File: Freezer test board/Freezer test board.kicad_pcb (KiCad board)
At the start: 4 copper layers, 89.9 x 104.9 mm, 18 parts, among them J1 TB007-508-03BE, J2 TB007-508-03BE, J3 TB007-508-03BE, J4 TB007-508-03BE, J5 TB007-508-03BE, J6 TB007-508-03BE, J7 Conn_02x20_Odd_Even, J8 Conn_02x02_Odd_Even

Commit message: temp commit
I just curved the edges of the PCB and un-did all the connection
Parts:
- H1, H2, H3, H4, J1, J2, J3, J4, J5, J6, J7, R1, R2, R3, R4, R5, R6: moved to F.Cu
- J8: moved to B.Cu
- moved H1 78.2 mm to (90.1, 40.7), turned to 0 degrees
- moved H2 78.2 mm to (90.1, 98.7), turned to 0 degrees
- moved J7 75.7 mm to (91.4, 45.6), turned to 0 degrees
- moved J1 73.4 mm to (165.9, 41.0)
- moved J2 73.4 mm to (165.9, 58.1)
- moved J3 73.4 mm to (165.9, 74.7)
- moved J4 73.4 mm to (165.9, 91.9)
- moved J5 73.4 mm to (165.9, 108.6)
- moved J6 73.4 mm to (165.9, 125.6)
- moved R1 38.1 mm to (148.3, 46.1), turned to 0 degrees
- moved R2 38.1 mm to (148.3, 63.2), turned to 0 degrees
- moved R3 38.1 mm to (148.3, 79.8), turned to 0 degrees
- moved R4 38.1 mm to (148.3, 97.0), turned to 0 degrees
- moved R5 38.1 mm to (148.3, 113.7), turned to 0 degrees
- moved R6 38.1 mm to (148.3, 130.7), turned to 0 degrees
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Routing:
- net 3V3: track 549.0 -> 0.33 mm
- net GND: track 510.4 -> 0.25 mm
- net GPIO26: track 72.8 -> 0.00 mm, vias 1 -> 0
- net GPIO6: track 69.0 -> 0.00 mm, vias 1 -> 0
- net GPIO22: track 63.3 -> 0.00 mm, vias 1 -> 0
- net GPIO5: track 63.1 -> 0.00 mm, vias 1 -> 0
- net GPIO17: track 61.6 -> 0.00 mm, vias 1 -> 0
- net GPIO27: track 57.5 -> 0.00 mm, vias 1 -> 0
- net Net-(J2-Signal): track 17.4 -> 0.00 mm, vias 1 -> 0
- net Net-(J1-Signal): track 17.3 -> 0.00 mm, vias 1 -> 0
- net Net-(J3-Signal): track 17.3 -> 0.00 mm, vias 1 -> 0
- net Net-(J4-Signal): track 17.3 -> 0.00 mm, vias 1 -> 0
- net Net-(J6-Signal): track 17.3 -> 0.00 mm, vias 1 -> 0
- net Net-(J5-Signal): track 17.3 -> 0.00 mm, vias 1 -> 0
- added copper zone on In2.Cu, net 3V3
- added copper zone on B.Cu, net GPIO17
- added copper zone on F.Cu, net GPIO17
- added copper zone on In1.Cu, net GPIO17
- removed copper zone on B.Cu, net GND
- removed copper zone on F.Cu, net GND
- removed copper zone on In1.Cu, net GND
- removed copper zone on In2.Cu, net GND
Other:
- outline, holes or cut-outs redrawn

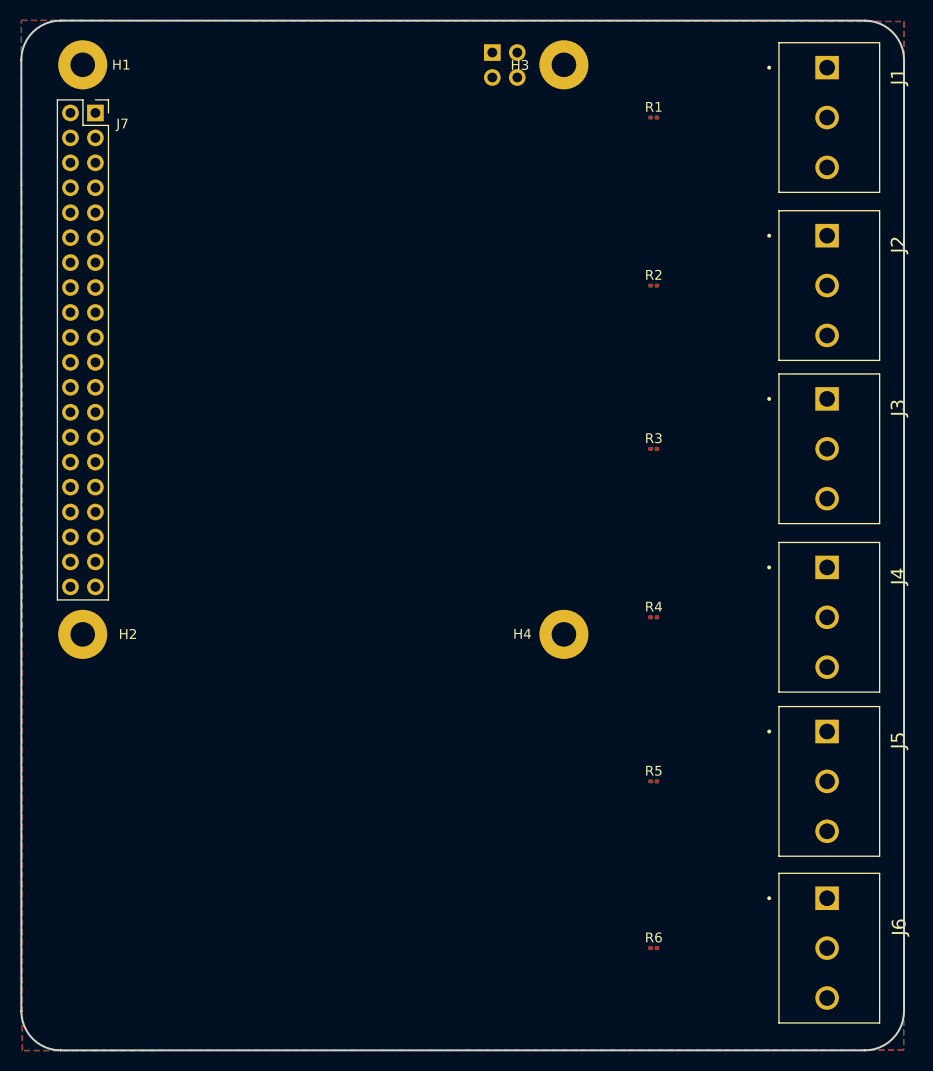
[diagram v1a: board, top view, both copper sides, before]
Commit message: Temporary Push
At the moment the most recent changes Made are the following: board has been shrunk by moving the terminal blocks in-between the mounting holes, the terminal blocks have been changed from 5.08mm to 3.54mm. The layers have been changed from SIG-GND-PWR-GND to SIG-GND-PWR-SIG2. Then all of the connections have been removed. No schematic changes
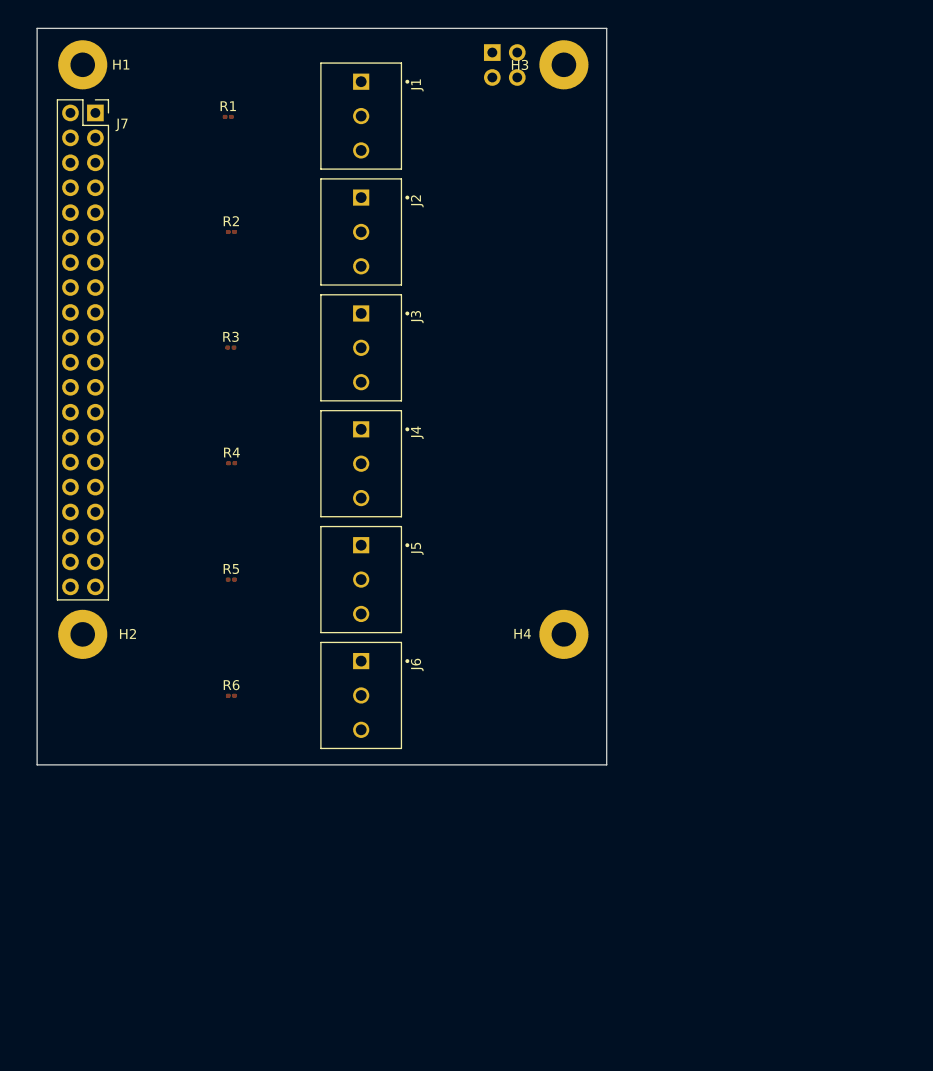
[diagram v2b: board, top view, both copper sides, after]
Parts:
- J1, J2, J3, J4, J5, J6: value TB007-508-03BE -> 284391-3; footprint TB007-508-03BE:CUI_TB007-508-03BE -> 284391_3:TE_284391-3
- moved J6 51.7 mm to (118.5, 104.9)
- moved R6 50.1 mm to (105.3, 105.0)
- moved J5 49.9 mm to (118.5, 93.1)
- moved J4 48.6 mm to (118.5, 81.3)
- moved J3 47.7 mm to (118.5, 69.5)
- moved J1 47.7 mm to (118.5, 45.9)
- moved R5 47.7 mm to (105.3, 93.1)
- moved J2 47.4 mm to (118.5, 57.7)
- moved R4 45.8 mm to (105.3, 81.3)
- moved R3 44.3 mm to (105.2, 69.5)
- moved R2 43.4 mm to (105.3, 57.7)
- moved R1 43.3 mm to (105.0, 46.0)
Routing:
- removed copper zone on In2.Cu, net 3V3
- removed copper zone on B.Cu, net GPIO17
- removed copper zone on F.Cu, net GPIO17
- removed copper zone on In1.Cu, net GPIO17
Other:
- board size 89.9 x 104.9 mm -> 58 x 75 mm

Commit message: Uh
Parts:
- moved R6 0.38 mm to (104.9, 104.8)
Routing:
- net 3V3: track 0.00 -> 204.9 mm
- net GND: track 0.00 -> 184.5 mm
- net GPIO26: track 0.00 -> 19.0 mm
- net GPIO17: track 0.00 -> 18.3 mm
- net GPIO6: track 0.00 -> 17.4 mm
- net GPIO22: track 0.00 -> 16.0 mm
- net GPIO27: track 0.00 -> 14.8 mm
- net GPIO5: track 0.00 -> 13.6 mm
- net Net-(J6-DATA): track 0.00 -> 13.3 mm
- net Net-(J1-DATA): track 0.00 -> 13.3 mm
- net Net-(J3-DATA): track 0.00 -> 13.0 mm
- net Net-(J5-DATA): track 0.00 -> 12.9 mm
- net Net-(J2-DATA): track 0.00 -> 12.9 mm
- net Net-(J4-DATA): track 0.00 -> 12.9 mm
- added copper zone on In2.Cu, net 3V3
- added copper zone on In1.Cu, net GND
- added copper zone on F.Cu, net GPIO26
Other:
- outline, holes or cut-outs redrawn

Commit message: changes layouts
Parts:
- removed J1: 284391-3, 284391_3:TE_284391-3
- removed the J2 at (118.5, 57.7)
- removed the R1 at (105.0, 46.0)
- added J7: 284391-3, 284391_3:TE_284391-3, F.Cu at (136.0, 73.5)
- added J9: 284391-3, 284391_3:TE_284391-3, F.Cu at (136.0, 49.5)
- added R3: 4.7k, Resistor_SMD:R_0201_0603Metric, F.Cu at (120.8, 48.8)
- added R7: 4.7k, Resistor_SMD:R_0201_0603Metric, F.Cu at (120.7, 87.7)
- J8: value Conn_02x02_Odd_Even -> 284391-3; footprint Connector_PinSocket_2.54mm:PinSocket_2x02_P2.54mm_Vertical -> 284391_3:TE_284391-3; moved to F.Cu
- moved R6 53.3 mm to (120.8, 54.0)
- moved J2 48.2 mm to (89.0, 93.7), turned to 180 degrees
- moved R5 43.7 mm to (120.8, 52.2)
- moved R4 34.5 mm to (120.8, 50.5)
- moved J3 32.1 mm to (101.0, 96.5), turned to 180 degrees
- moved J6 26.1 mm to (136.0, 85.5)
- moved R2 25.6 mm to (128.5, 47.0)
- moved J8 22.4 mm to (136.0, 61.5), turned to -90 degrees
- moved R1 18.9 mm to (120.5, 58.3)
- moved J4 16.1 mm to (113.0, 96.5), turned to 180 degrees
- moved J5 7.32 mm to (125.0, 96.5), turned to 180 degrees
- moved H4 1.16 mm to (138.0, 98.5)
- moved H1 1.16 mm to (89.0, 40.5)
- moved H2 1.16 mm to (89.0, 98.5)
- moved H3 1.15 mm to (138.0, 40.7)
- renumbered J7 to J2, R3 to R1
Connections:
- J2 pad 1: 3V3 -> +3V3
- J3 pad 1: 3V3 -> +3V3
- J3 pad 2: Net-(J3-DATA) -> GPIO17
- J4 pad 1: 3V3 -> +3V3
- J4 pad 2: Net-(J4-DATA) -> GPIO27
- J5 pad 1: 3V3 -> +3V3
- J5 pad 2: Net-(J5-DATA) -> GPIO22
- J6 pad 1: 3V3 -> +3V3
- J6 pad 2: Net-(J6-DATA) -> GPIO5
- J8 pad 1: unconnected-(J8-Pin_1-Pad1) -> +3V3
- J8 pad 2: unconnected-(J8-Pin_2-Pad2) -> GPIO26
- J8 pad 3: unconnected-(J8-Pin_3-Pad3) -> GND
- R1 pad 1: GPIO22 -> GPIO17
- R1 pad 2: Net-(J3-DATA) -> +3V3
- R2 pad 2: Net-(J2-DATA) -> +3V3
- R4 pad 2: Net-(J4-DATA) -> +3V3
- R5 pad 2: Net-(J5-DATA) -> +3V3
- R6 pad 2: Net-(J6-DATA) -> +3V3
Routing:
- net 3V3: track 204.9 -> 0.00 mm
- net GND: track 184.5 -> 0.00 mm
- net GPIO26: track 19.0 -> 0.00 mm
- net GPIO17: track 18.3 -> 0.00 mm
- net GPIO6: track 17.4 -> 0.00 mm
- net GPIO22: track 16.0 -> 0.00 mm
- net GPIO27: track 14.8 -> 0.00 mm
- net GPIO5: track 13.6 -> 0.00 mm
- net Net-(J6-DATA): track 13.3 -> 0.00 mm
- net Net-(J1-DATA): track 13.3 -> 0.00 mm
- net Net-(J3-DATA): track 13.0 -> 0.00 mm
- net Net-(J5-DATA): track 12.9 -> 0.00 mm
- net Net-(J2-DATA): track 12.9 -> 0.00 mm
- net Net-(J4-DATA): track 12.9 -> 0.00 mm
- added copper zone on In2.Cu, net +3V3
- added copper zone on F.Cu, net GND
- removed copper zone on In2.Cu, net 3V3
- removed copper zone on F.Cu, net GPIO26
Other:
- board size 58 x 75 mm -> 56 x 65 mm

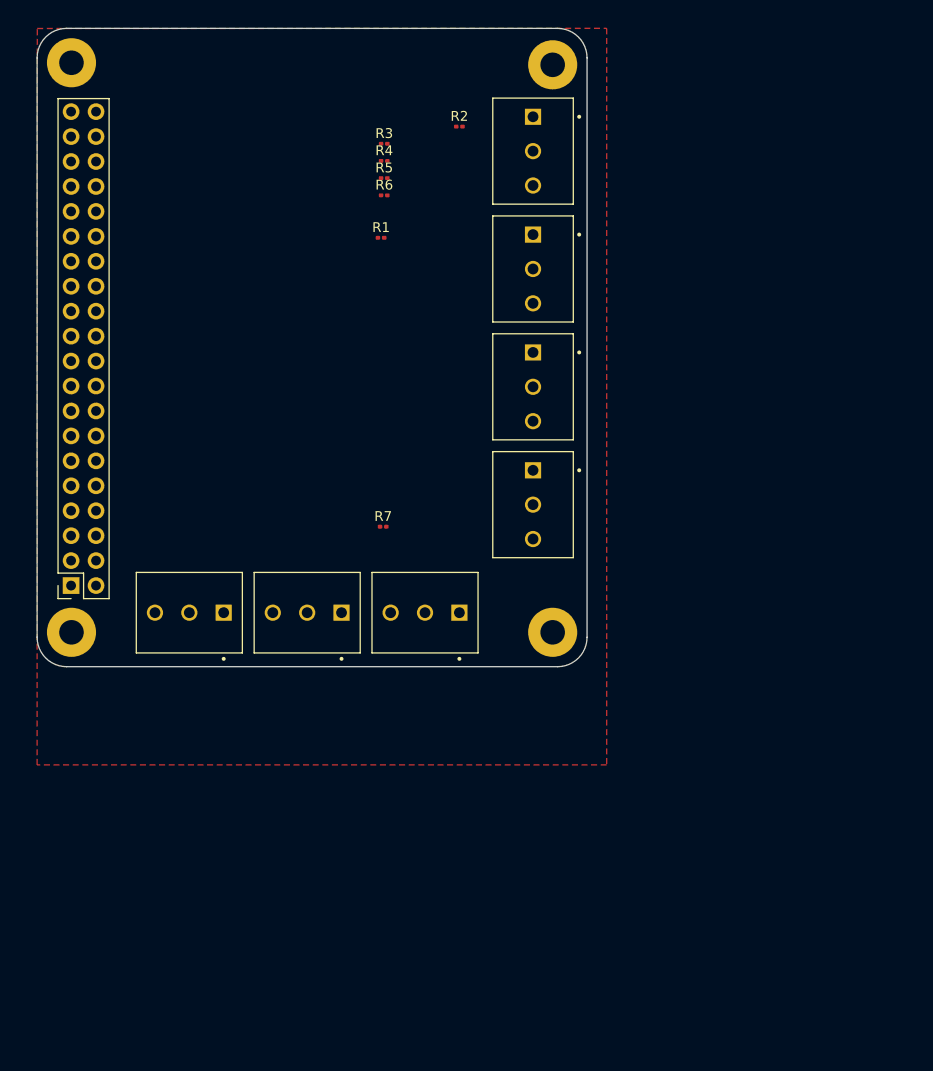
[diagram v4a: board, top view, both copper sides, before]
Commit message: Changed to 1 GPIO and cleaned up the connections
All of the Signals connections have been changed to go to One GPIO pin per the request of the software person. connections were cleaned up because they were all over the place.
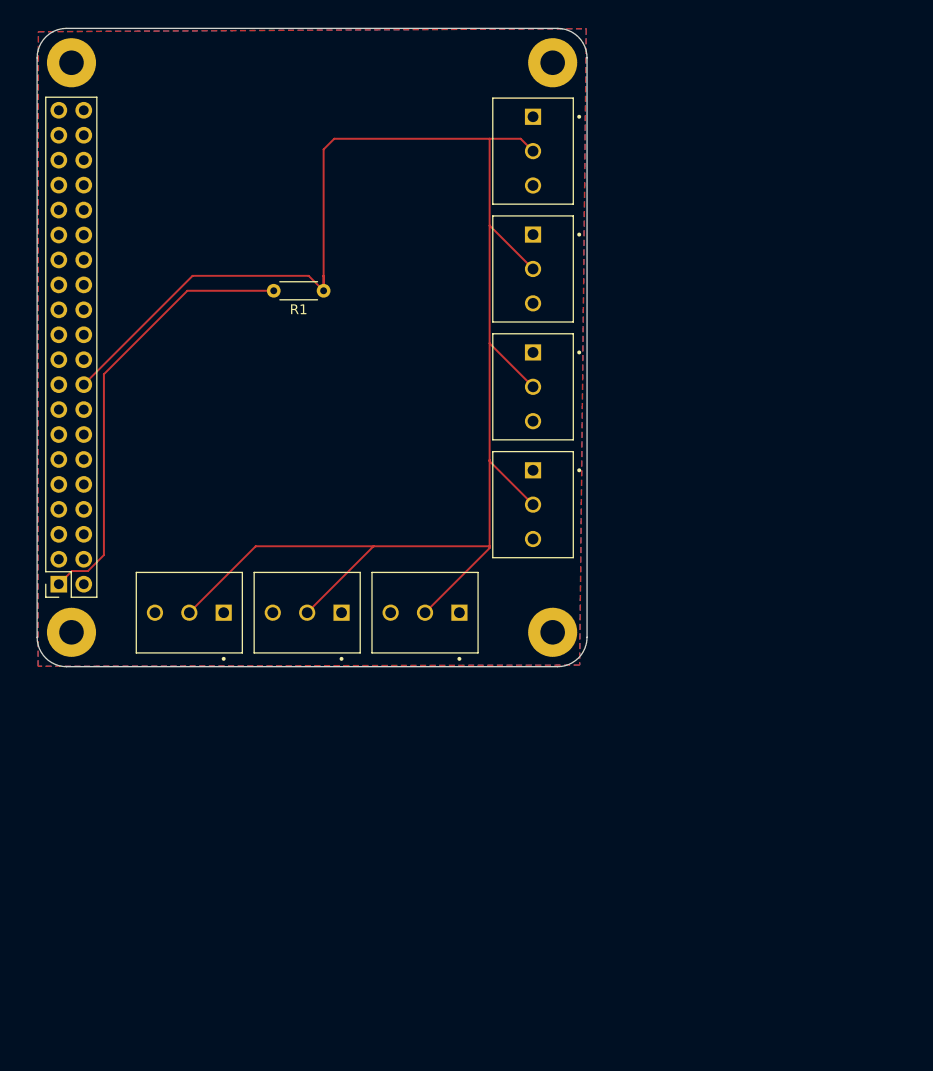
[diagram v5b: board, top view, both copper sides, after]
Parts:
- removed R2, R3, R4, R5, R6, R7: 4.7k, Resistor_SMD:R_0201_0603Metric
- R1: footprint Resistor_SMD:R_0201_0603Metric -> Resistor_THT:R_Axial_DIN0204_L3.6mm_D1.6mm_P5.08mm_Horizontal
- moved R1 7.96 mm to (114.7, 63.7), turned to 180 degrees
- moved J2 1.26 mm to (87.7, 93.6)
- moved H3 0.21 mm to (138.0, 40.5)
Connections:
- J2 pad 11: GPIO17 -> unconnected-(J2-Pin_11-Pad11)
- J2 pad 13: GPIO27 -> unconnected-(J2-Pin_13-Pad13)
- J2 pad 14: unconnected-(J2-Pin_14-Pad14) -> GND
- J2 pad 15: GPIO22 -> unconnected-(J2-Pin_15-Pad15)
- J2 pad 18: unconnected-(J2-Pin_18-Pad18) -> GPIO24
- J2 pad 20: unconnected-(J2-Pin_20-Pad20) -> GND
- J2 pad 29: GPIO5 -> unconnected-(J2-Pin_29-Pad29)
- J2 pad 30: unconnected-(J2-Pin_30-Pad30) -> GND
- J2 pad 31: GPIO6 -> unconnected-(J2-Pin_31-Pad31)
- J2 pad 34: unconnected-(J2-Pin_34-Pad34) -> GND
- J2 pad 37: GPIO26 -> unconnected-(J2-Pin_37-Pad37)
- J2 pad 39: GND -> unconnected-(J2-Pin_39-Pad39)
- J2 pad 6: unconnected-(J2-Pin_6-Pad6) -> GND
- J3 pad 2: GPIO17 -> GPIO24
- J4 pad 2: GPIO27 -> GPIO24
- J5 pad 2: GPIO22 -> GPIO24
- J6 pad 2: GPIO5 -> GPIO24
- J7 pad 2: GPIO6 -> GPIO24
- J8 pad 2: GPIO26 -> GPIO24
- J9 pad 2: GPIO26 -> GPIO24
- R1 pad 1: GPIO17 -> GPIO24
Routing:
- net GPIO24: track 0.00 -> 181.4 mm
- net GND: track 0.00 -> 174.1 mm
- net +3V3: track 0.00 -> 162.5 mm
- added copper zone on B.Cu, net GND
